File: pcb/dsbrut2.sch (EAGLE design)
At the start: 18 parts, among them IC1 4175D, IC2 74HC125D, IC3 MEGA8-AI, Y1 X1

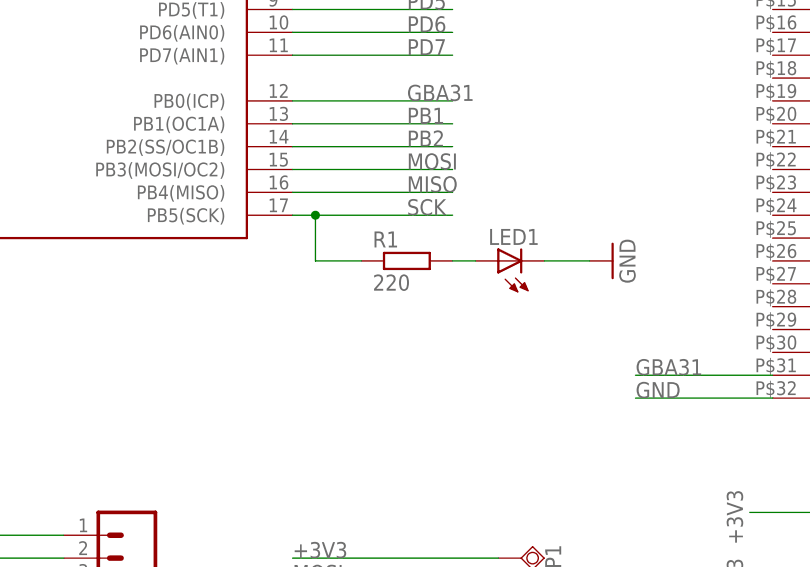
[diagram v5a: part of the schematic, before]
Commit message: changed soldermask of gba2 bridge, added gerber files, added CAM file for dsbrut2, zip file for order in sexy bash script
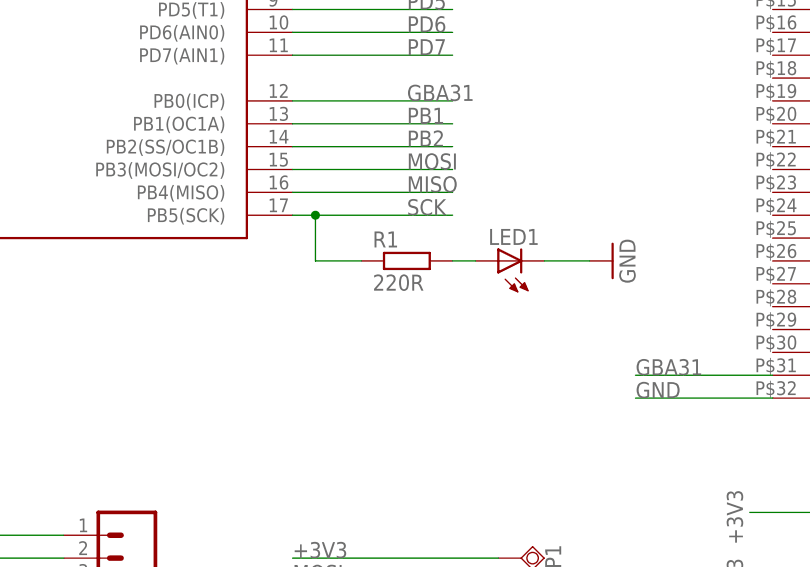
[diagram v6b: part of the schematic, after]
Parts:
- R1: value 220 -> 220R
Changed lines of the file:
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@@
 <part name="LED1" library="SparkFunEagle-6-6-07" deviceset="LED" device="0603"/>
 <part name="GND3" library="supply1" deviceset="GND" device=""/>
-<part name="R1" library="rcl" deviceset="R-EU_" device="M0805" value="220"/>
+<part name="R1" library="rcl" deviceset="R-EU_" device="M0805" value="220R"/>
 <part name="VSS1" library="supply1" deviceset="VSS" device=""/>
 <part name="F1" library="dp_devices" deviceset="INDUCTOR" device="-L1812" value="F1"/>
